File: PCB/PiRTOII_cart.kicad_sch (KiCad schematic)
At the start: 6 parts, among them J1 2x22 card edge connector, J2 Conn_01x20, J3 Conn_01x20, Q1 BC547, SW1 SW_Push

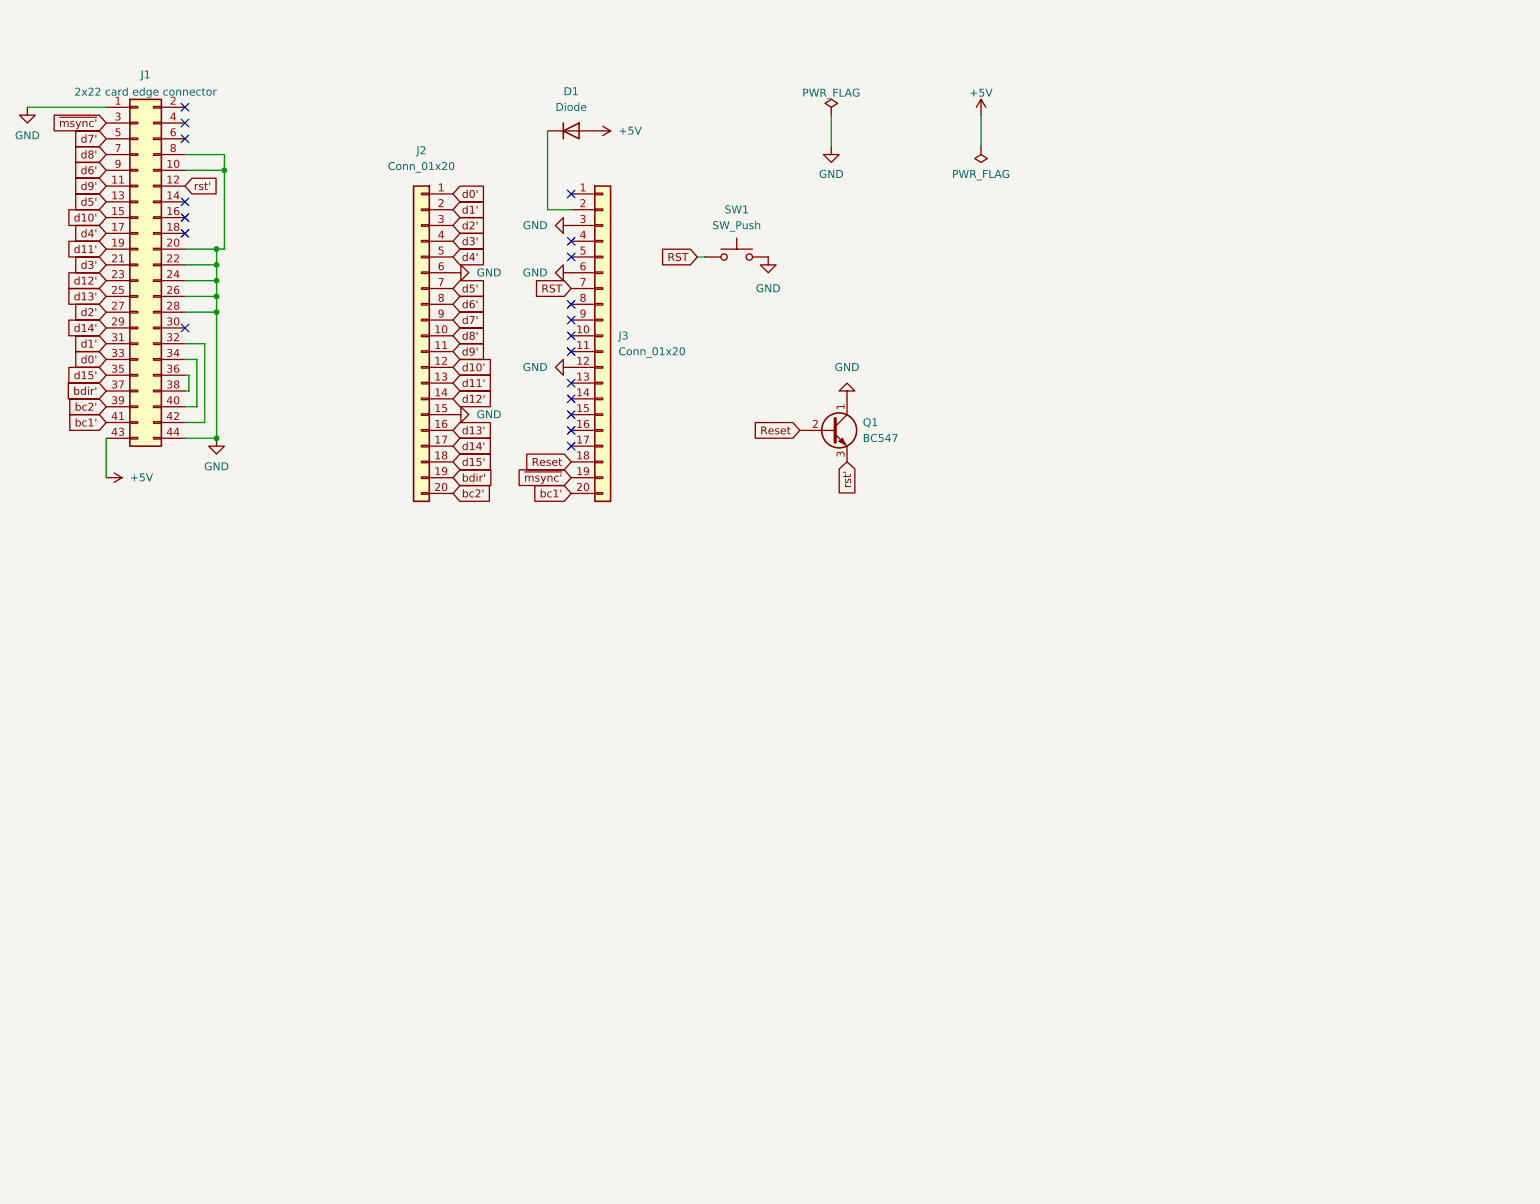
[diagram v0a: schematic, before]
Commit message: Use original Pico board
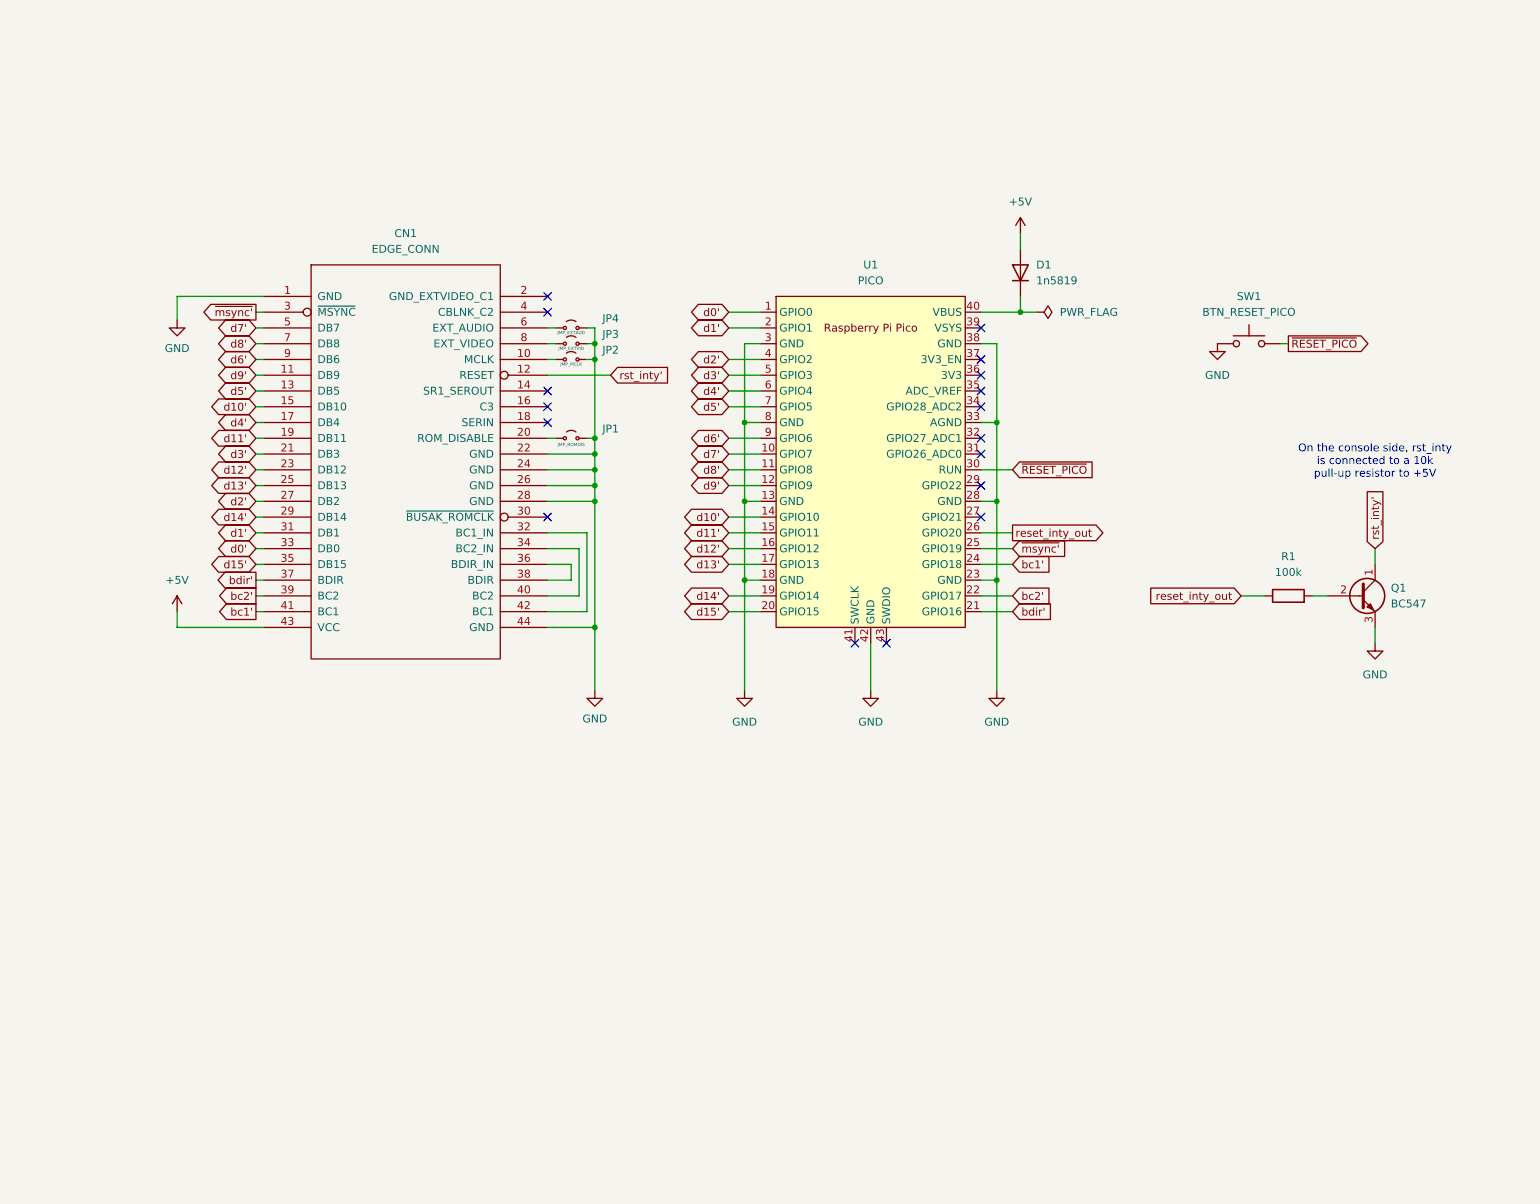
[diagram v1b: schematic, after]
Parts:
- removed J1: 2x22 card edge connector, Evan's misc parts:edge mounted 44 pin card edge connector (2x22 pin), symbol Evan's misc parts:2x22 card edge connector
- removed J2, J3: Conn_01x20, Connector_PinSocket_2.54mm:PinSocket_1x20_P2.54mm_Vertical, symbol Connector_Generic:Conn_01x20
- added CN1: EDGE_CONN, PiRTOII:Intellivision_Edge_Connector, symbol INTELLIVISION_CART_CONN:INTELLIVISION_CART_CONN
- added JP1: JMP_ROMDIS, Jumper:SolderJumper-2_P1.3mm_Open_RoundedPad1.0x1.5mm, symbol Jumper:Jumper_2_Small_Open
- added JP2: JMP_MCLK, Jumper:SolderJumper-2_P1.3mm_Open_RoundedPad1.0x1.5mm, symbol Jumper:Jumper_2_Small_Open
- added JP3: JMP_EXTVID, Jumper:SolderJumper-2_P1.3mm_Open_RoundedPad1.0x1.5mm, symbol Jumper:Jumper_2_Small_Open
- added JP4: JMP_EXTAUD, Jumper:SolderJumper-2_P1.3mm_Open_RoundedPad1.0x1.5mm, symbol Jumper:Jumper_2_Small_Open
- added R1: 100k, Resistor_THT:R_Axial_DIN0207_L6.3mm_D2.5mm_P10.16mm_Horizontal, symbol Device:R
- added U1: PICO, MCU_RaspberryPi_and_Boards:RPi_Pico_SMD_TH, symbol MCU_RaspberryPi_and_Boards:Pico
- D1: value Diode -> 1n5819; footprint Diode_THT:D_DO-35_SOD27_P7.62mm_Horizontal -> Diode_THT:D_DO-41_SOD81_P10.16mm_Horizontal
- SW1: value SW_Push -> BTN_RESET_PICO
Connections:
- net RST is gone; now on net GND: SW1.1
- net rst' is gone; now on net GND: Q1.3 (E)
- net +5V: now also CN1.43 (VCC)
- net GND: now also CN1.1 (GND), CN1.22 (GND), CN1.24 (GND), CN1.26 (GND), CN1.28 (GND), CN1.44 (GND), JP1.2 (B), JP2.2 (B), JP3.2 (B), JP4.2 (B), U1.13 (GND), U1.18 (GND), U1.23 (GND), U1.28 (GND), U1.3 (GND), U1.33 (AGND), U1.38 (GND), U1.42 (GND), U1.8 (GND); no longer Q1.1 (C), SW1.2
- net bc1': now also CN1.41 (BC1), U1.24 (GPIO18)
- net bc2': now also CN1.39 (BC2), U1.22 (GPIO17)
- net bdir': now also CN1.37 (BDIR), U1.21 (GPIO16)
- net d0': now also CN1.33 (DB0), U1.1 (GPIO0)
- net d1': now also CN1.31 (DB1), U1.2 (GPIO1)
- net d10': now also CN1.15 (DB10), U1.14 (GPIO10)
- net d11': now also CN1.19 (DB11), U1.15 (GPIO11)
- net d12': now also CN1.23 (DB12), U1.16 (GPIO12)
- net d13': now also CN1.25 (DB13), U1.17 (GPIO13)
- net d14': now also CN1.29 (DB14), U1.19 (GPIO14)
- net d15': now also CN1.35 (DB15), U1.20 (GPIO15)
- net d2': now also CN1.27 (DB2), U1.4 (GPIO2)
- net d3': now also CN1.21 (DB3), U1.5 (GPIO3)
- net d4': now also CN1.17 (DB4), U1.6 (GPIO4)
- net d5': now also CN1.13 (DB5), U1.7 (GPIO5)
- net d6': now also CN1.9 (DB6), U1.9 (GPIO6)
- net d7': now also CN1.5 (DB7), U1.10 (GPIO7)
- net d8': now also CN1.7 (DB8), U1.11 (GPIO8)
- net d9': now also CN1.11 (DB9), U1.12 (GPIO9)
- net ~{msync'}: now also CN1.3 (~{MSYNC}), U1.25 (GPIO19)
- net at D1.1 (K): now also U1.40 (VBUS)
- net Reset: no longer names the net of Q1.2 (B)
- net Reset: now also R1.2
- new net: CN1.6 (EXT_AUDIO), JP4.1 (A)
- new net: CN1.8 (EXT_VIDEO), JP3.1 (A)
- new net: CN1.10 (MCLK), JP2.1 (A)
- new net: CN1.20 (ROM_DISABLE), JP1.1 (A)
- new net: CN1.32 (BC1_IN), CN1.42 (BC1)
- new net: CN1.34 (BC2_IN), CN1.40 (BC2)
- new net: CN1.36 (BDIR_IN), CN1.38 (BDIR)
- new net reset_inty_out: R1.1, U1.26 (GPIO20)
- new net rst_inty': CN1.12 (RESET), Q1.1 (C)
- new net ~{RESET_PICO}: SW1.2, U1.30 (RUN)
- no-connect marks 19 -> 17
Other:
- note added: "On the console side, rst_inty is connected to a 10k pull-up resistor to +5V"
- moved on the sheet: Q1, SW1

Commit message: Almost there
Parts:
- added J1: CONN_SNOOP, Connector_PinHeader_2.54mm:PinHeader_2x22_P2.54mm_Vertical, symbol Connector_Generic:Conn_02x22_Odd_Even
- added U2, U3, U4: 74LVC245, Package_DIP:DIP-20_W7.62mm_Socket_LongPads, symbol 74xx:74LS245
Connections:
- net +5V: now also J1.43 (Pin_43)
- net GND: now also J1.1 (Pin_1), J1.22 (Pin_22), J1.24 (Pin_24), J1.26 (Pin_26), J1.28 (Pin_28), J1.44 (Pin_44), U2.10 (GND), U2.19 (CE), U3.10 (GND), U3.19 (CE), U4.10 (GND), U4.19 (CE)
- net bc1': now also CN1.32 (BC1_IN), CN1.42 (BC1), J1.32 (Pin_32), J1.41 (Pin_41), J1.42 (Pin_42), U4.4 (A2); no longer U1.24 (GPIO18)
- net bc2': now also CN1.34 (BC2_IN), CN1.40 (BC2), J1.34 (Pin_34), J1.39 (Pin_39), J1.40 (Pin_40), U4.3 (A1); no longer U1.22 (GPIO17)
- net bdir': now also CN1.36 (BDIR_IN), CN1.38 (BDIR), J1.36 (Pin_36), J1.37 (Pin_37), J1.38 (Pin_38), U4.2 (A0); no longer U1.21 (GPIO16)
- net d0': now also J1.33 (Pin_33), U2.2 (A0); no longer U1.1 (GPIO0)
- net d1': now also J1.31 (Pin_31), U2.3 (A1); no longer U1.2 (GPIO1)
- net d10': now also J1.15 (Pin_15), U3.4 (A2); no longer U1.14 (GPIO10)
- net d11': now also J1.19 (Pin_19), U3.5 (A3); no longer U1.15 (GPIO11)
- net d12': now also J1.23 (Pin_23), U3.6 (A4); no longer U1.16 (GPIO12)
- net d13': now also J1.25 (Pin_25), U3.7 (A5); no longer U1.17 (GPIO13)
- net d14': now also J1.29 (Pin_29), U3.8 (A6); no longer U1.19 (GPIO14)
- net d15': now also J1.35 (Pin_35), U3.9 (A7); no longer U1.20 (GPIO15)
- net d2': now also J1.27 (Pin_27), U2.4 (A2); no longer U1.4 (GPIO2)
- net d3': now also J1.21 (Pin_21), U2.5 (A3); no longer U1.5 (GPIO3)
- net d4': now also J1.17 (Pin_17), U2.6 (A4); no longer U1.6 (GPIO4)
- net d5': now also J1.13 (Pin_13), U2.7 (A5); no longer U1.7 (GPIO5)
- net d6': now also J1.9 (Pin_9), U2.8 (A6); no longer U1.9 (GPIO6)
- net d7': now also J1.5 (Pin_5), U2.9 (A7); no longer U1.10 (GPIO7)
- net d8': now also J1.7 (Pin_7), U3.2 (A0); no longer U1.11 (GPIO8)
- net d9': now also J1.11 (Pin_11), U3.3 (A1); no longer U1.12 (GPIO9)
- net rst_inty': now also J1.12 (Pin_12)
- net ~{msync'}: now also J1.3 (Pin_3), U4.5 (A3); no longer U1.25 (GPIO19)
- net ext_audio: now reaches CN1.6 (EXT_AUDIO), JP4.1 (A)
- net ext_audio: now also J1.6 (Pin_6)
- net DIR: now reaches U1.34 (GPIO28_ADC2)
- net DIR: now also U2.1 (A->B), U3.1 (A->B)
- net +3.3V: now reaches U1.36 (3V3)
- net +3.3V: now also U2.20 (VCC), U3.20 (VCC), U4.1 (A->B), U4.20 (VCC)
- net ext_video: now reaches CN1.8 (EXT_VIDEO), JP3.1 (A)
- net ext_video: now also J1.8 (Pin_8)
- net mclk: now reaches CN1.10 (MCLK), JP2.1 (A)
- net mclk: now also J1.10 (Pin_10)
- net sr1: now reaches CN1.14 (SR1_SEROUT)
- net sr1: now also J1.14 (Pin_14)
- net c3: now reaches CN1.16 (C3)
- net c3: now also J1.16 (Pin_16)
- net serin: now reaches CN1.18 (SERIN)
- net serin: now also J1.18 (Pin_18)
- net c1: now reaches CN1.2 (GND_EXTVIDEO_C1)
- net c1: now also J1.2 (Pin_2)
- net rom_disable: now reaches CN1.20 (ROM_DISABLE), JP1.1 (A)
- net rom_disable: now also J1.20 (Pin_20)
- net ~{busak}: now reaches CN1.30 (~{BUSAK_ROMCLK})
- net ~{busak}: now also J1.30 (Pin_30)
- net c2: now reaches CN1.4 (CBLNK_C2)
- net c2: now also J1.4 (Pin_4)
- new net bc1_lv: U1.24 (GPIO18), U4.16 (B2)
- new net bc2_lv: U1.22 (GPIO17), U4.17 (B1)
- new net bdir_lv: U1.21 (GPIO16), U4.18 (B0)
- new net d0_lv: U1.1 (GPIO0), U2.18 (B0)
- new net d10_lv: U1.14 (GPIO10), U3.16 (B2)
- new net d11_lv: U1.15 (GPIO11), U3.15 (B3)
- new net d12_lv: U1.16 (GPIO12), U3.14 (B4)
- new net d13_lv: U1.17 (GPIO13), U3.13 (B5)
- new net d14_lv: U1.19 (GPIO14), U3.12 (B6)
- new net d15_lv: U1.20 (GPIO15), U3.11 (B7)
- new net d1_lv: U1.2 (GPIO1), U2.17 (B1)
- new net d2_lv: U1.4 (GPIO2), U2.16 (B2)
- new net d3_lv: U1.5 (GPIO3), U2.15 (B3)
- new net d4_lv: U1.6 (GPIO4), U2.14 (B4)
- new net d5_lv: U1.7 (GPIO5), U2.13 (B5)
- new net d6_lv: U1.9 (GPIO6), U2.12 (B6)
- new net d7_lv: U1.10 (GPIO7), U2.11 (B7)
- new net d8_lv: U1.11 (GPIO8), U3.18 (B0)
- new net d9_lv: U1.12 (GPIO9), U3.17 (B1)
- new net ~{msync_lv}: U1.25 (GPIO19), U4.15 (B3)
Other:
- note added: "3.3V is generated on the Pico board (Max 300 mA)"
- note added: "A->B when HIGH"
- company: Andrea Ottaviani -> Andrea Ottaviani/SukkoPera
- title: RTO-Multicart -> PiRTO II Cart - "Official Pico" Edition
- moved on the sheet: CN1, D1, JP1, JP2, JP3, JP4, Q1, R1, SW1, U1

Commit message: Add MicroSD slot
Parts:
- added CN2: MICRO_SD_SLOT, PiRTOII:GCT-MEM2055-00-190-01-A, symbol Connector:Micro_SD_Card_Det2
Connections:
- net +3.3V: now also CN2.4 (VDD)
- net GND: now also CN2.1 (DAT2), CN2.10 (DET_A), CN2.11 (SHIELD), CN2.6 (VSS), CN2.8 (DAT1)
- net bc1_lv: now also U1.31 (GPIO26_ADC0); no longer U1.24 (GPIO18)
- net bc2_lv: now also U1.32 (GPIO27_ADC1); no longer U1.22 (GPIO17)
- net bdir_lv: now also U1.29 (GPIO22); no longer U1.21 (GPIO16)
- net ~{msync_lv}: now also U1.27 (GPIO21); no longer U1.25 (GPIO19)
- new net CS: CN2.2 (DAT3/CD), U1.22 (GPIO17)
- new net MISO: CN2.7 (DAT0), U1.21 (GPIO16)
- new net MOSI: CN2.3 (CMD), U1.25 (GPIO19)
- new net SCK: CN2.5 (CLK), U1.24 (GPIO18)
- no-connect marks 17 -> 14
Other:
- moved on the sheet: U2, U3, U4

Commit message: Use better BJT footprint
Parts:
- Q1: footprint Package_TO_SOT_THT:TO-92_Inline -> Package_TO_SOT_THT:TO-92_HandSolder
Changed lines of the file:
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@@
 			)
 		)
-		(property "Footprint" "Package_TO_SOT_THT:TO-92_Inline"
+		(property "Footprint" "Package_TO_SOT_THT:TO-92_HandSolder"
 			(at 233.68 147.955 0)
 			(effects
